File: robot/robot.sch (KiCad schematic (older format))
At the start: 0 parts

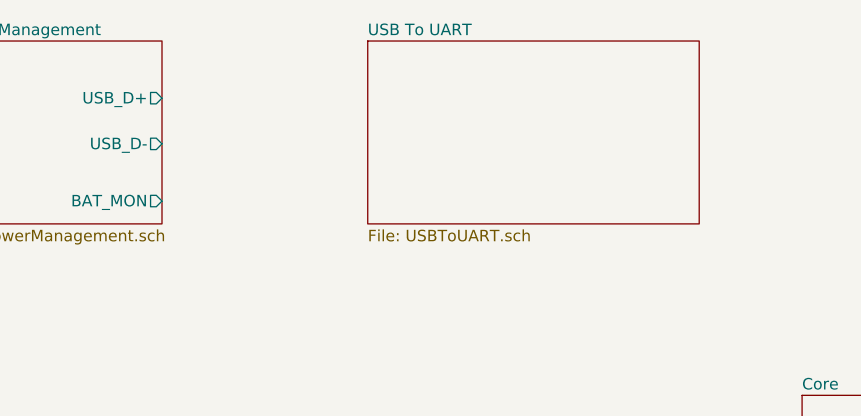
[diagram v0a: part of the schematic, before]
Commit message: USB to UART + autoreset
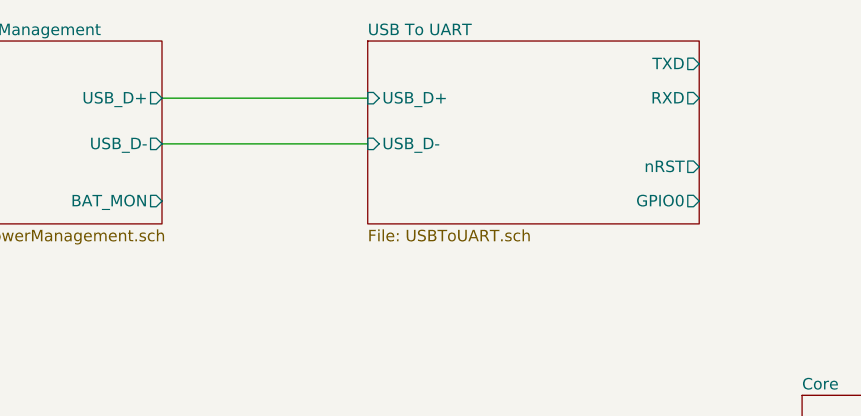
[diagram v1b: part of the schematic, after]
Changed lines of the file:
@@
 F0 "USB To UART" 50
 F1 "USBToUART.sch" 50
+F2 "USB_D+" I L 2650 1150 50
+F3 "USB_D-" I L 2650 1350 50
+F4 "TXD" O R 4100 1000 50
+F5 "RXD" O R 4100 1150 50
+F6 "nRST" O R 4100 1450 50
+F7 "GPIO0" O R 4100 1600 50
 $EndSheet
+Wire Wire Line
+	1750 1150 2650 1150
+Wire Wire Line
+	1750 1350 2650 1350
 $EndSCHEMATC

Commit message: Object detection, reset
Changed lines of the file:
@@
 $Descr A4 11693 8268
 encoding utf-8
-Sheet 1 4
+Sheet 1 5
 Title "Micro Sumo"
 Date "2019-06-28"
@@
 $EndSheet
 $Sheet
-S 4550 2450 850  750
+S 4550 2450 1350 1500
 U 5D179377
 F0 "Core" 50
 F1 "Core.sch" 50
+F2 "TXD" I L 4550 2600 50
+F3 "RXD" I L 4550 2750 50
+F4 "GPIO0" I L 4550 3100 50
+F5 "EN" I L 4550 2950 50
+F6 "SDA_1" B L 4550 3300 50
+F7 "SCL_1" O L 4550 3450 50
 $EndSheet
 $Sheet
@@
 Wire Wire Line
 	1750 1350 2650 1350
+Wire Wire Line
+	4500 1000 4500 2600
+Wire Wire Line
+	4500 2600 4550 2600
+Wire Wire Line
+	4100 1000 4500 1000
+Wire Wire Line
+	4100 1150 4400 1150
+Wire Wire Line
+	4400 1150 4400 2750
+Wire Wire Line
+	4400 2750 4550 2750
+Wire Wire Line
+	4250 1450 4250 2950
+Wire Wire Line
+	4250 2950 4550 2950
+Wire Wire Line
+	4100 1450 4250 1450
+Wire Wire Line
+	4100 1600 4150 1600
+Wire Wire Line
+	4150 1600 4150 3100
+Wire Wire Line
+	4150 3100 4550 3100
+$Sheet
+S 1750 3950 1150 1250
+U 5D6361BC
+F0 "Object Detection" 50
+F1 "Object Detection.sch" 50
+F2 "OD_INTERRUPT" O R 2900 4400 50
+F3 "OD_SHUT" I R 2900 4600 50
+F4 "OD_SCL" I R 2900 4050 50
+F5 "OD_SDA" B R 2900 4200 50
+$EndSheet
+Wire Wire Line
+	2900 4050 4100 4050
+Wire Wire Line
+	4100 4050 4100 3450
+Wire Wire Line
+	4100 3450 4550 3450
+Wire Wire Line
+	2900 4200 3950 4200
+Wire Wire Line
+	3950 4200 3950 3300
+Wire Wire Line
+	3950 3300 4550 3300
 $EndSCHEMATC
